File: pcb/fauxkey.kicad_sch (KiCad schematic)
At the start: 3 parts, among them J1 Conn_ARM_SWD_TagConnect_TC203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, U1 E73-2G4M08S1C, Y1 32.768 kHz

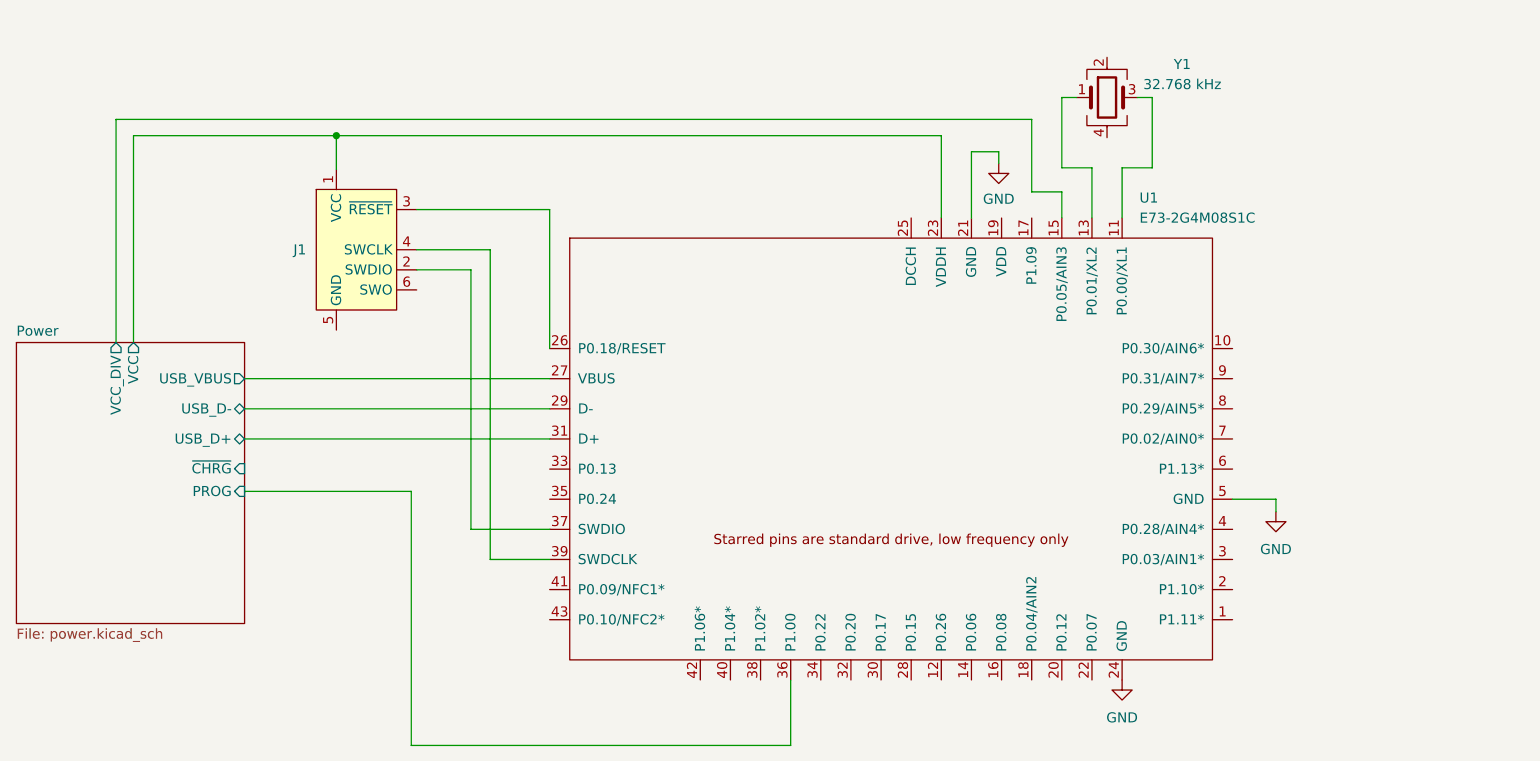
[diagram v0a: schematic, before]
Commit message: PCB v0.2
Changes:
  - Fix the crystal footprint to be for 32.768 kHz crystals, not MHz
  - Add load capacitors to crystal
  - Make the footprint for the battery wires larger
  - Mark the positive pin on the battery pins
  - Remove extraneous footprint labels
  - Fix island in module ground plane
  - Resize pad connection holes to support Mill Max 0850
  - Resize mounting holes to match the actual PCB
  - Connect both sides of the cutout for rigidity
  - Allow mounting the USB-C connector on either side of the PCB
  - Replace Tag-Connect footprint with the cable I actually have
  - Move all used pins to the outside of the module
  - Break out a pair of unused pins for UART or whatever
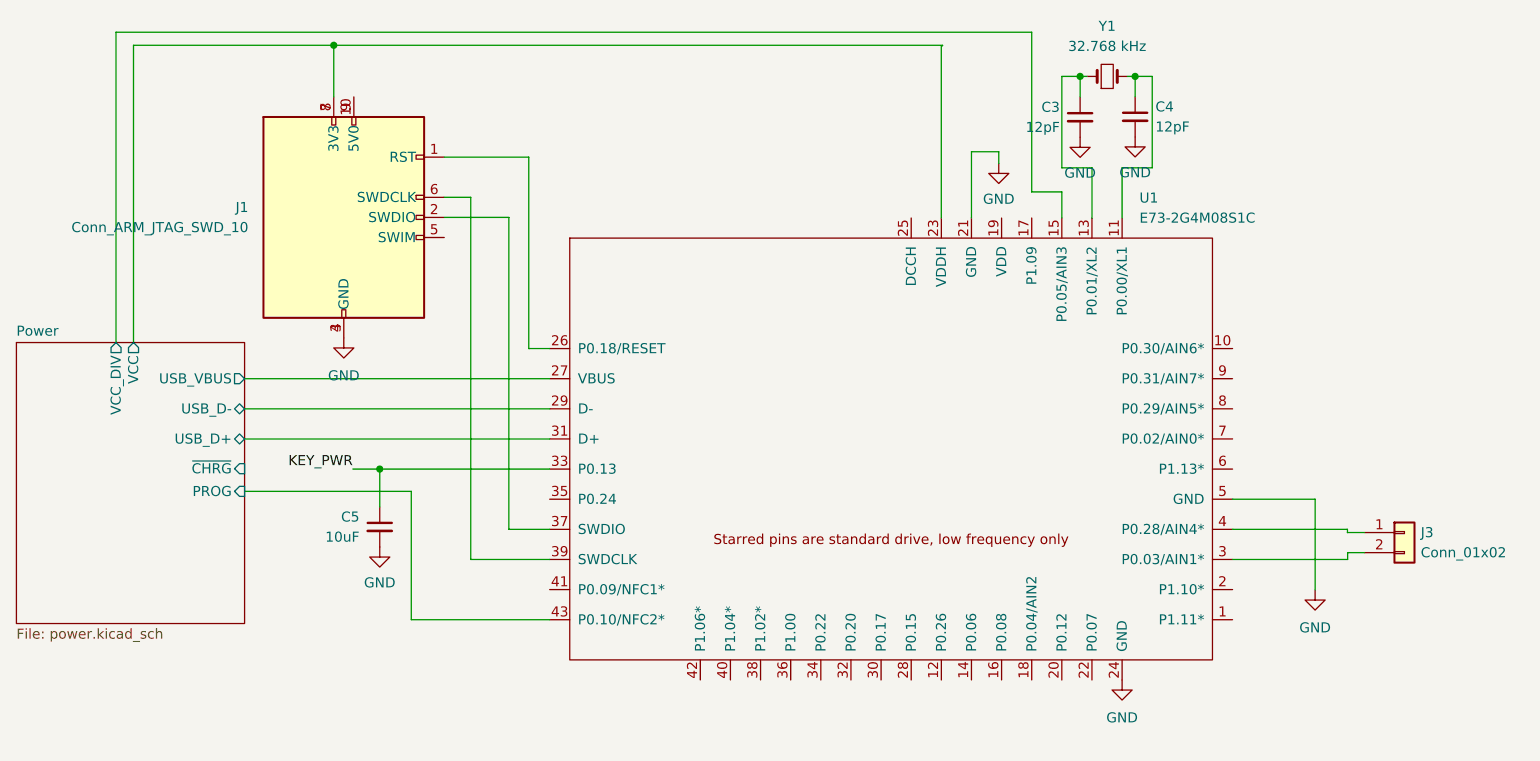
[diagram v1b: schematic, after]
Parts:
- removed J1: Conn_ARM_SWD_TagConnect_TC2030-NL, Connector:Tag-Connect_TC2030-IDC-NL_2x03_P1.27mm_Vertical, symbol Connector:Conn_ARM_SWD_TagConnect_TC2030-NL
- added C3, C4: 12pF, Capacitor_SMD:C_0603_1608Metric, symbol Device:C_Small
- added C5: 10uF, Capacitor_SMD:C_0603_1608Metric, symbol Device:C_Small
- added J1: Conn_ARM_JTAG_SWD_10, Connector:Tag-Connect_TC2050-IDC-NL_2x05_P1.27mm_Vertical, symbol fauxkey:Conn_ARM_SWD-TC2050-STLink-Clone
- added J3: Conn_01x02, Connector_PinHeader_2.00mm:PinHeader_1x02_P2.00mm_Vertical, symbol Connector_Generic:Conn_01x02
- Y1: footprint Crystal:Crystal_SMD_3225-4Pin_3.2x2.5mm -> Crystal:Crystal_SMD_3215-2Pin_3.2x1.5mm; symbol Device:Crystal_GND24 -> Device:Crystal_Small
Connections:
- net GND: now also C3.2, C4.2, C5.2, J1.3 (GND), J1.4 (GND)
- net Power/PROG: now also U1.43 (P0.10/NFC2*); no longer U1.36 (P1.00)
- net Power/VCC: now also J1.7 (3V3), J1.8 (3V3)
- net at U1.37 (SWDIO): now also J1.2 (SWDIO)
- net at U1.26 (P0.18/RESET): now also J1.1 (RST)
- net at U1.39 (SWDCLK): now also J1.6 (SWDCLK)
- net at U1.11 (P0.00/XL1): now also Y1.2, C4.1; no longer Y1.3
- net at U1.13 (P0.01/XL2), Y1.1: now also C3.1
- net at U1.3 (P0.03/AIN1*): now also J3.2 (Pin_2)
- net KEY_PWR: now reaches U1.33 (P0.13)
- net KEY_PWR: now also C5.1
- net at U1.4 (P0.28/AIN4*): now also J3.1 (Pin_1)
- new net: J1.10 (5V0), J1.9 (5V0)
